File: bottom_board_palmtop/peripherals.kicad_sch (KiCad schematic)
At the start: 51 parts, among them J45 SH 2P, Q14 2N7002DW-7-F, Q19 2N7002DW-7-F, Q2 2N7002DW-7-F, SW10 ON/OFF, SW11 EVQPUL02K, SW4 ON/OFF, SW5 ON/OFF, SW6 ON/OFF, SW7 EVQPUL02K, SW8 EVQPUL02K, SW9 EVQPUL02K, U34 TMP102xxDRL, U38 PCF85363ATT, U40 BL24C32A, U42 TPAZ1043-04F, Y3 SC-20S,32.768kHz,20PPM,7pF

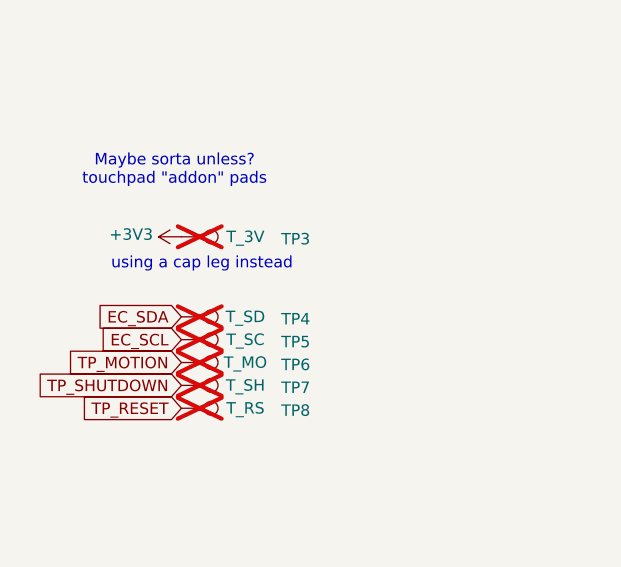
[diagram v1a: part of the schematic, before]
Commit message: adding project logo and reorganizing silk, adding 5v testpoint to touchpad module +a few tiny track tweaks
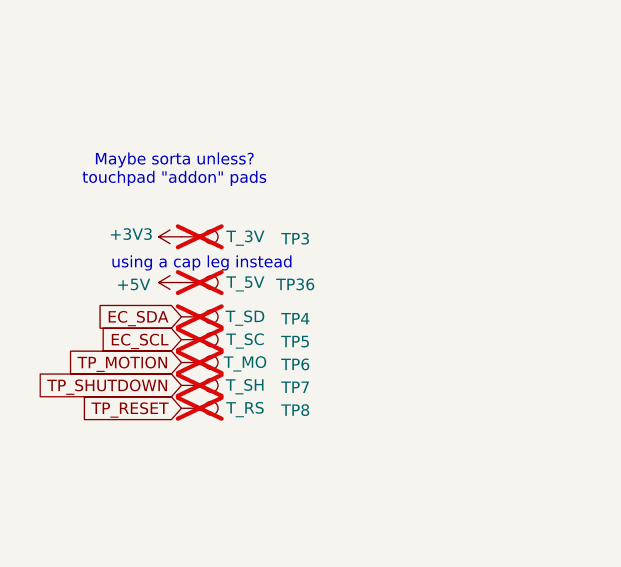
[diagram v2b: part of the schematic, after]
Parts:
- added TP36: T_5V, bottom_board_palmtop:TestPoint_Pad_0.6x0.6mm, symbol Connector:TestPoint
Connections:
- net +5V: now also TP36.1
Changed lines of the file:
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@@
+	)
+	(symbol
+		(lib_id "Connector:TestPoint")
+		(at 31.75 76.2 270)
+		(unit 1)
+		(exclude_from_sim no)
+		(in_bom no)
+		(on_board yes)
+		(dnp yes)
+		(property "Reference" "TP36"
+			(at 44.45 76.454 90)
+			(effects
+				(font
+					(size 1.27 1.27)
+				)
+			)
+		)
+		(property "Value" "T_5V"
+			(at 38.862 76.2 90)
+			(effects
+				(font
+					(size 1.27 1.27)
+				)
+			)
+		)
+		(property "Footprint" "bottom_board_palmtop:TestPoint_Pad_0.6x0.6mm"
+			(at 31.75 81.28 0)
+			(effects
+				(font
+					(size 1.27 1.27)
+				)
+				(hide yes)
+			)
+		)
+		(property "Datasheet" "~"
+			(at 31.75 81.28 0)
+			(effects
+				(font
+					(size 1.27 1.27)
+				)
+				(hide yes)
+			)
+		)
+		(property "Description" "test point"
+			(at 31.75 76.2 0)
+			(effects
+				(font
+					(size 1.27 1.27)
+				)
+				(hide yes)
+			)
+		)
+		(property "Alternatives" ""
+			(at 31.75 76.2 90)
+			(effects
+				(font
+					(size 1.27 1.27)
+				)
+				(hide yes)
+			)
+		)
+		(pin "1"
+		)
+		(instances
+			(project "bottom_board_palmtop"
+				(path "/8978b49f-2e56-47e1-8d7c-c31ed8b7a8ae/0c6b5fa6-e988-4584-9433-105aa03f0fd6"
+					(reference "TP36")
+					(unit 1)
+				)
+			)
+		)
 	)
 	(symbol
@@
 					(unit 1)
 				)
+			)
+		)
+	)
+	(symbol
+		(lib_id "power:+5V")
+		(at 31.75 76.2 90)
+		(unit 1)
+		(exclude_from_sim no)
+		(in_bom yes)
+		(on_board yes)
+		(dnp no)
+		(property "Reference" "#PWR0147"
+			(at 35.56 76.2 0)
+			(effects
+				(font
+					(size 1.27 1.27)
+				)
+				(hide yes)
+			)
+		)
+		(property "Value" "+5V"
+			(at 26.416 76.454 90)
+			(effects
+				(font
+					(size 1.27 1.27)
+				)
+			)
+		)
+		(property "Footprint" ""
+			(at 31.75 76.2 0)
+			(effects
+				(font
+					(size 1.27 1.27)
+				)
+				(hide yes)
+			)
+		)
+		(property "Datasheet" ""
+			(at 31.75 76.2 0)
+			(effects
+				(font
+					(size 1.27 1.27)
+				)
+				(hide yes)
+			)
+		)
+		(property "Description" ""
+			(at 31.75 76.2 0)
+			(effects
+				(font
+					(size 1.27 1.27)
+				)
+				(hide yes)
+			)
+		)
+		(pin "1"
+		)
+		(instances
+			(project "bottom_board_palmtop"
+				(path "/8978b49f-2e56-47e1-8d7c-c31ed8b7a8ae/0c6b5fa6-e988-4584-9433-105aa03f0fd6"
+					(reference "#PWR0147")
+					(unit 1)
+				)

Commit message: changing JST-SH 2p connectors to vertical, poking board art around and adding more
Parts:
- J45: footprint Connector_JST:JST_SH_SM02B-SRSS-TB_1x02-1MP_P1.00mm_Horizontal -> Connector_JST:JST_SH_BM02B-SRSS-TB_1x02-1MP_P1.00mm_Vertical
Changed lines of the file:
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@@
 			)
 		)
-		(property "Footprint" "Connector_JST:JST_SH_SM02B-SRSS-TB_1x02-1MP_P1.00mm_Horizontal"
+		(property "Footprint" "Connector_JST:JST_SH_BM02B-SRSS-TB_1x02-1MP_P1.00mm_Vertical"
 			(at 92.71 180.34 0)
 			(effects
